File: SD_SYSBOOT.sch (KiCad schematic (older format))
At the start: 18 parts

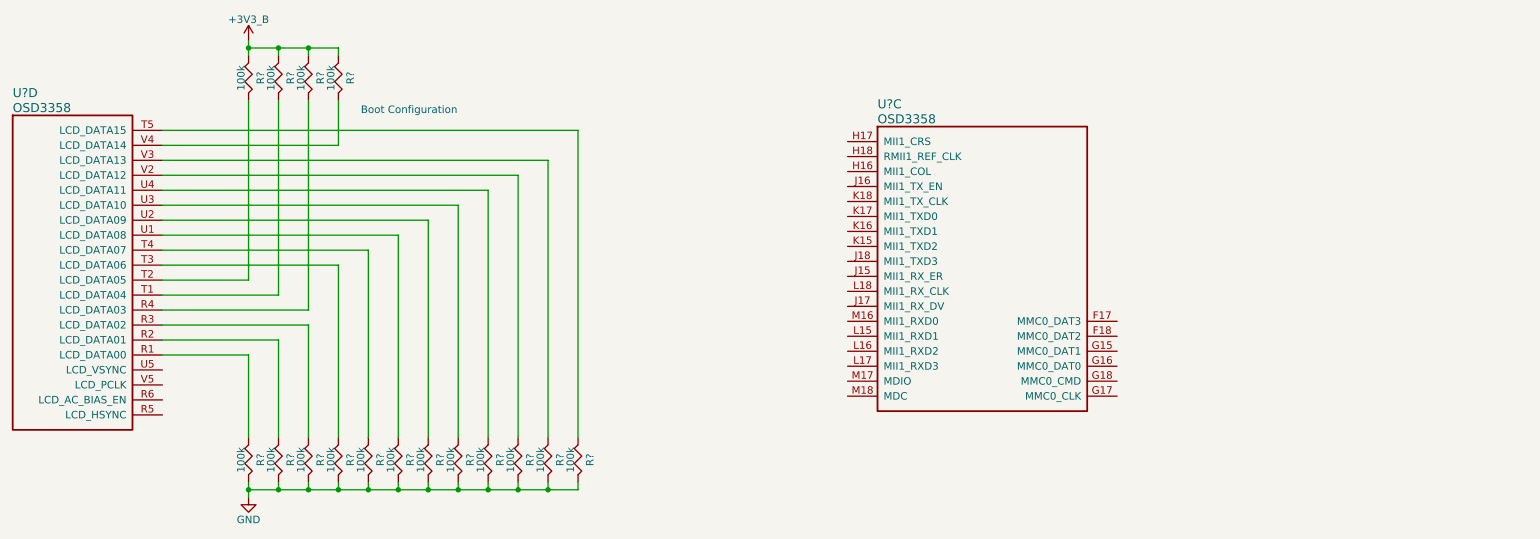
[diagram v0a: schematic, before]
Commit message: Added micro SD
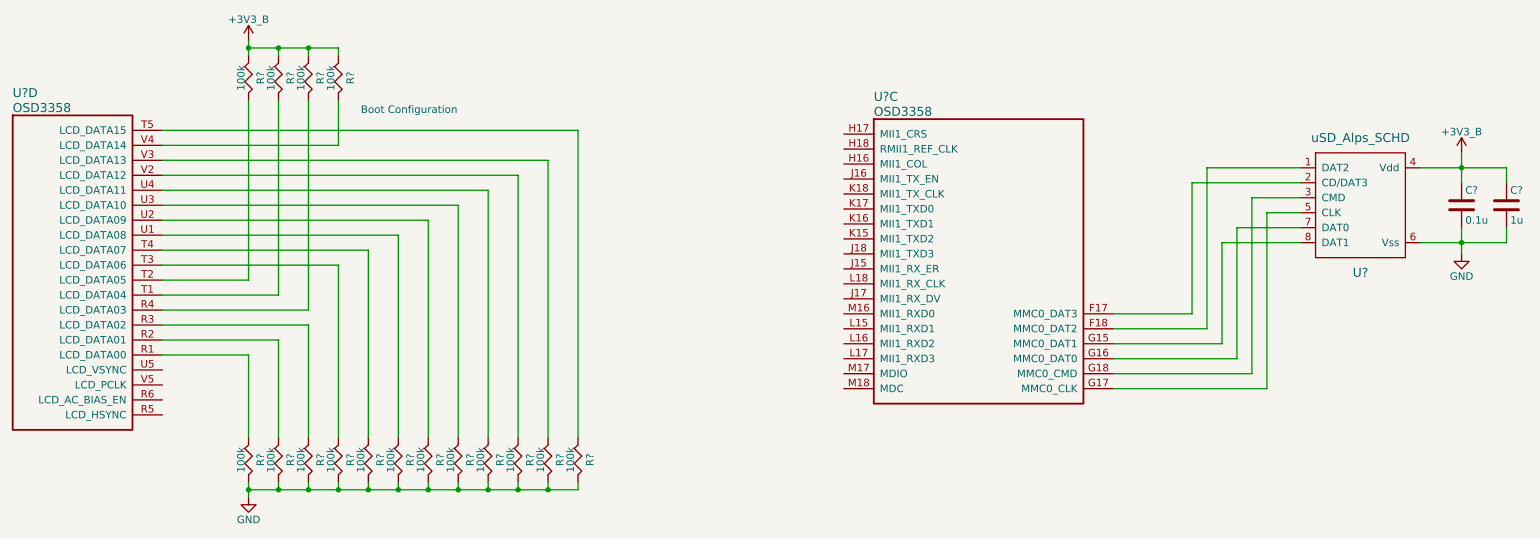
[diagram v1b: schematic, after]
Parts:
- added C?: 0.1u, symbol C
- added C?: 1u, symbol C
- added U?: uSD_Alps_SCHD, symbol uSD_Alps_SCHD
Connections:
- net +3V3_B: now also C?.1, C?.1, U?.4 (Vdd)
- net GND: now also C?.2, C?.2, U?.6 (Vss)
- net at U?.F17 (MMC0_DAT3): now also U?.2 (CD/DAT3)
- net at U?.F18 (MMC0_DAT2): now also U?.1 (DAT2)
- net at U?.G15 (MMC0_DAT1): now also U?.8 (DAT1)
- net at U?.G16 (MMC0_DAT0): now also U?.7 (DAT0)
- net at U?.G17 (MMC0_CLK): now also U?.5 (CLK)
- net at U?.G18 (MMC0_CMD): now also U?.3 (CMD)
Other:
- moved on the sheet: U?C
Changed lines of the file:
@@
 L OSD3358 U?
 U 3 1 573A6A27
-P 6500 1525
-F 0 "U?" H 6700 1775 60  0000 L CNN
-F 1 "OSD3358" H 6700 1675 60  0000 L CNN
-F 2 "" H 6500 1525 50  0000 C CNN
-F 3 "" H 6500 1525 50  0000 C CNN
-	3    6500 1525
+P 6475 1475
+F 0 "U?" H 6675 1725 60  0000 L CNN
+F 1 "OSD3358" H 6675 1625 60  0000 L CNN
+F 2 "" H 6475 1475 50  0000 C CNN
+F 3 "" H 6475 1475 50  0000 C CNN
+	3    6475 1475
 	1    0    0    -1
 $EndComp
@@
 Text Notes 3250 1350 0    50   ~ 0
 Boot Configuration
+$Comp
+L uSD_Alps_SCHD U?
+U 1 1 573BDA66
+P 9925 1950
+F 0 "U?" H 9925 1500 60  0000 C CNN
+F 1 "uSD_Alps_SCHD" H 9925 2400 60  0000 C CNN
+F 2 "" H 9925 1950 60  0000 C CNN
+F 3 "" H 9925 1950 60  0000 C CNN
+	1    9925 1950
+	1    0    0    -1
+$EndComp
+Wire Wire Line
+	8275 2675 8800 2675
+Wire Wire Line
+	8800 2675 8800 1800
+Wire Wire Line
+	8800 1800 9525 1800
+Wire Wire Line
+	8275 2775 8900 2775
+Wire Wire Line
+	8900 2775 8900 1700
+Wire Wire Line
+	8900 1700 9525 1700
+Wire Wire Line
+	8275 2875 9000 2875
+Wire Wire Line
+	9000 2875 9000 2200
+Wire Wire Line
+	9000 2200 9525 2200
+Wire Wire Line
+	8275 2975 9100 2975
+Wire Wire Line
+	9100 2975 9100 2100
+Wire Wire Line
+	9100 2100 9525 2100
+Wire Wire Line
+	8275 3075 9200 3075
+Wire Wire Line
+	9200 3075 9200 1900
+Wire Wire Line
+	9200 1900 9525 1900
+Wire Wire Line
+	8275 3175 9300 3175
+Wire Wire Line
+	9300 3175 9300 2000
+Wire Wire Line
+	9300 2000 9525 2000
+$Comp
+L C C?
+U 1 1 573BDF6B
+P 10600 1950
+F 0 "C?" H 10625 2050 50  0000 L CNN
+F 1 "0.1u" H 10625 1850 50  0000 L CNN
+F 2 "" H 10638 1800 50  0000 C CNN
+F 3 "" H 10600 1950 50  0000 C CNN
+	1    10600 1950
+	1    0    0    -1
+$EndComp
+Wire Wire Line
+	10325 1700 10900 1700
+Wire Wire Line
+	10600 1600 10600 1800
+Wire Wire Line
+	10325 2200 10900 2200
+Wire Wire Line
+	10600 2100 10600 2275
+Connection ~ 10600 2200
+$Comp
+L GND #PWR?
+U 1 1 573BE112
+P 10600 2275
+F 0 "#PWR?" H 10600 2025 50  0001 C CNN
+F 1 "GND" H 10600 2125 50  0000 C CNN
+F 2 "" H 10600 2275 50  0000 C CNN
+F 3 "" H 10600 2275 50  0000 C CNN
+	1    10600 2275
+	1    0    0    -1
+$EndComp
+Connection ~ 10600 1700
+$Comp
+L +3V3_B #PWR?
+U 1 1 573BE1BD
+P 10600 1600
+F 0 "#PWR?" H 10600 1450 50  0001 C CNN
+F 1 "+3V3_B" H 10600 1740 50  0000 C CNN
+F 2 "" H 10600 1600 50  0000 C CNN
+F 3 "" H 10600 1600 50  0000 C CNN
+	1    10600 1600
+	1    0    0    -1
+$EndComp
+$Comp
+L C C?
+U 1 1 573BEF84
+P 10900 1950
+F 0 "C?" H 10925 2050 50  0000 L CNN
+F 1 "1u" H 10925 1850 50  0000 L CNN
+F 2 "" H 10938 1800 50  0000 C CNN
+F 3 "" H 10900 1950 50  0000 C CNN
+	1    10900 1950
+	1    0    0    -1
+$EndComp
+Wire Wire Line
+	10900 1700 10900 1800
+Wire Wire Line
+	10900 2200 10900 2100
 $EndSCHEMATC
